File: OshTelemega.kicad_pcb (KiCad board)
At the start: 4 copper layers, 30 x 80 mm, 156 parts, among them J1 TAGCONNECT, J10 SERVOS, J2 Conn_01x02, J3 SMA_Edgelaunch, J4 USB_C_Receptacle_USB2.0_16P, J5 UFL, J6 RIGHT, J7 LEFT, J8 BATT, J9 Conn_02x05_Counter_Clockwise, Q1 SiA449DJ, Q2 AO3400A, Q3 SiA449DJ, Q4 SiA449DJ, U1 STM32L151VCTx, U10 MMC5983MA, U11 TSM200N03, U12 LM293QT, U13 LM293QT, U14 TSM200N03, U15 LM293QT, U16 TSM200N03, U17 MCP73831-2-OT, U18 TC2185-3.3VxCTTR, U19 W25Q64JVXGIQ, U2 WE-TVS-82400102, U21 SN74LVC1G80QDCKTQ1, U3 ADXL375, U4 MS5607-02BA, U5 MAX-M10S, U6 MCP130-xxxxTT, U7 DRV5012AEDMRR, U8 CC1200, U9 BMI088, X2 ECS-160-8-36Q-AES-TR1, Y1 ABM8W-40.0000MHZ

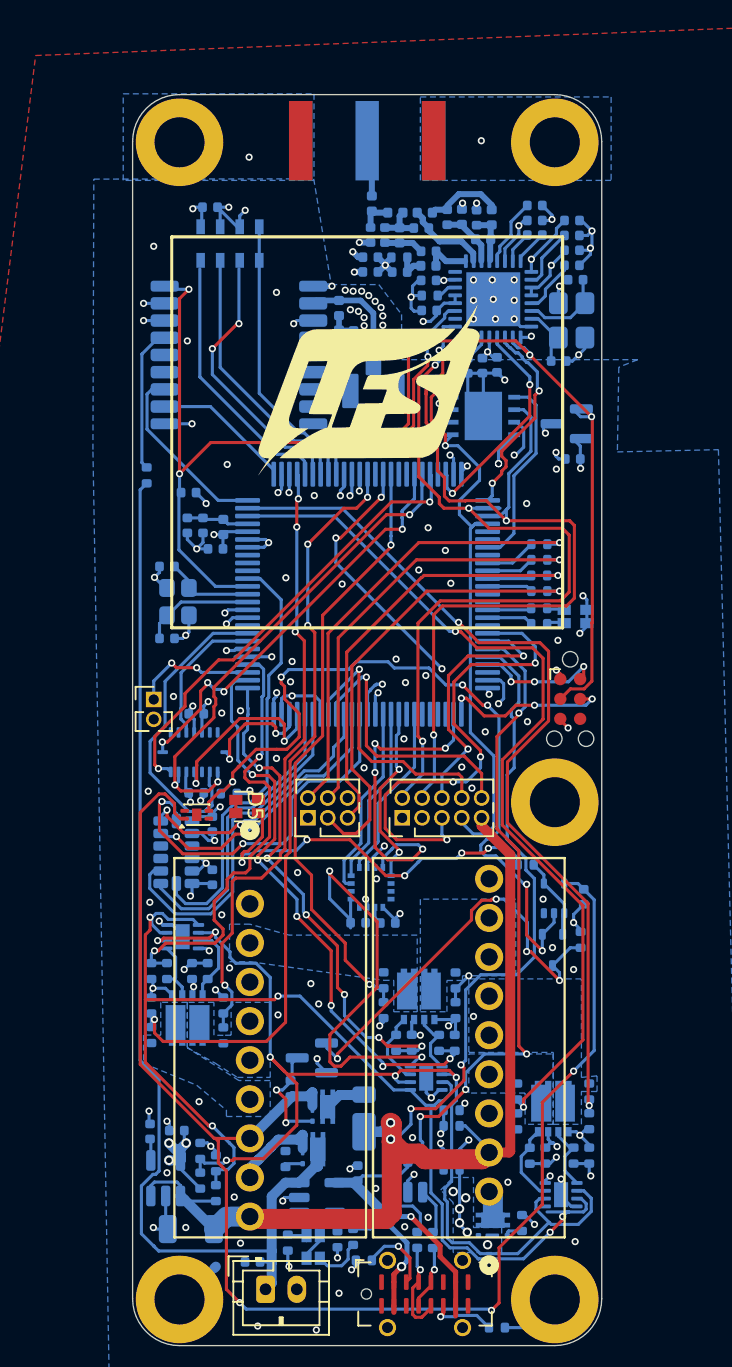
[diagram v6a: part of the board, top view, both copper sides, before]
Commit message: expanded SMA connector and added some more silkscreens
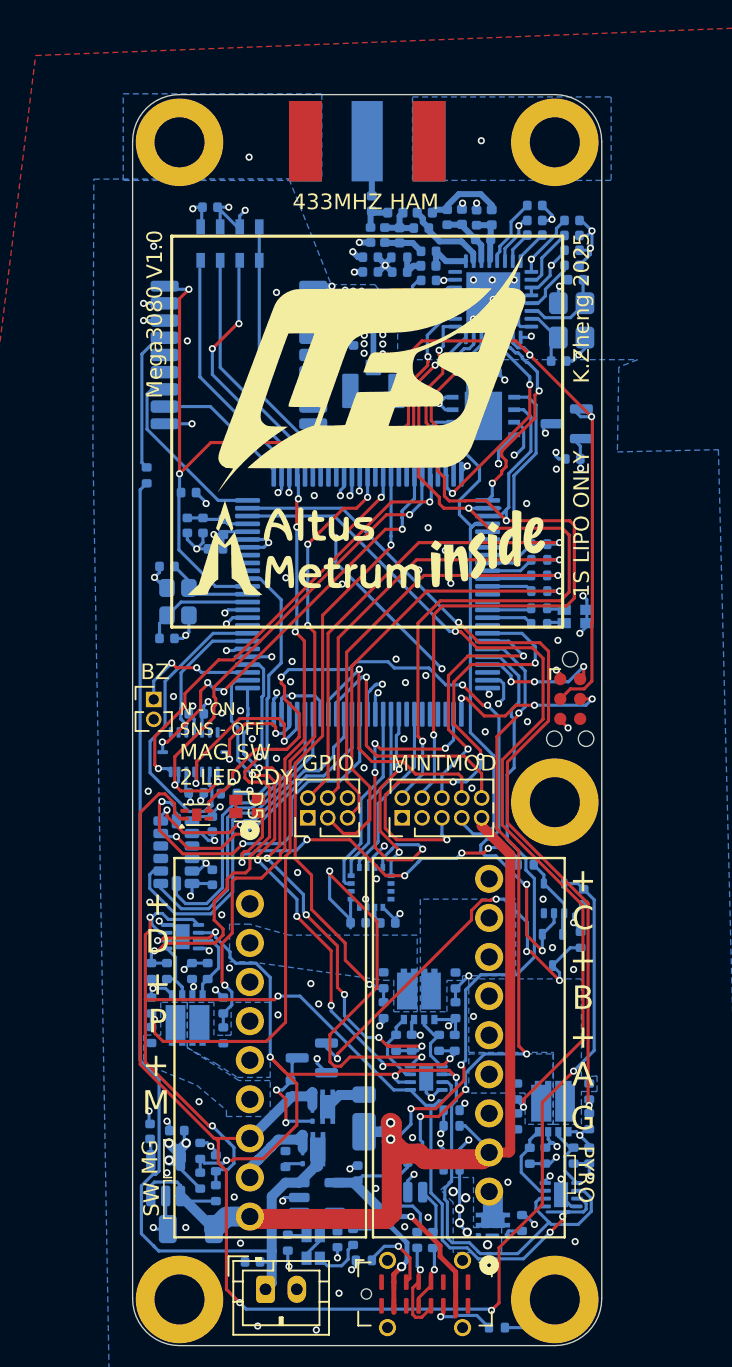
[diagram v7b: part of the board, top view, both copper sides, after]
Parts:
- removed the G*** at (34.9, 39.0)
- added G***: LOGO, LOGO, F.Cu at (35.0, 38.0)
- added G***: LOGO, LOGO, F.Cu at (35.0, 49.0)
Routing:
- net Net-(R10-Pad2): track 2.56 -> 3.69 mm
- net GND: track 124.0 -> 123.8 mm, vias 152 -> 151
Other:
- board text added: "+ A"
- board text added: "+ B"
- board text added: "+ C"
- board text added: "+ D"
- board text added: "+ G"
- board text added: "+ M"
- board text added: "+ O T 3V G"
- board text added: "+ P"
- board text added: "- +"
- board text added: "0 1 R I CK"
- board text added: "1S LIPO ONLY"
- board text added: "433MHZ HAM"
- board text added: "BZ"
- board text added: "D C G"
- board text added: "G"
- board text added: "G B A"
- board text added: "GPIO"
- board text added: "K.Zheng 2025"
- board text added: "L1/L5 GPS"
- board text added: "MAG SW 2 LED RDY"
- board text added: "MG"
- board text added: "MINTMOD"
- board text added: "Mega3080 V1.0"
- board text added: "N - ON SNS - OFF"
- board text added: "PYRO"
- board text added: "SW"
